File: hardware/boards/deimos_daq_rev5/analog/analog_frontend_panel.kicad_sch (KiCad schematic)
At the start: 17 parts, among them IC3001 BD42540FJ-CE2, IC3002 BD42540FJ-CE2, IC3003 BD42540FJ-CE2, J3001 Screw_Terminal_01x12, J3002 Screw_Terminal_01x10, J3003 Screw_Terminal_01x12, J3004 Screw_Terminal_01x12, J3005 Screw_Terminal_01x10, J3006 Screw_Terminal_01x12

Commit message: put +/12V on all inamps. add 3.3V zener behind first resistor of each filter.
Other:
- note added: "G=659+2/3"
- note removed: "G=666+1/3"
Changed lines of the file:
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@@
 		)
 	)
-	(text "G=666+1/3"
+	(text "G=659+2/3"
 		(exclude_from_sim no)
 		(at 265.684 70.866 0)

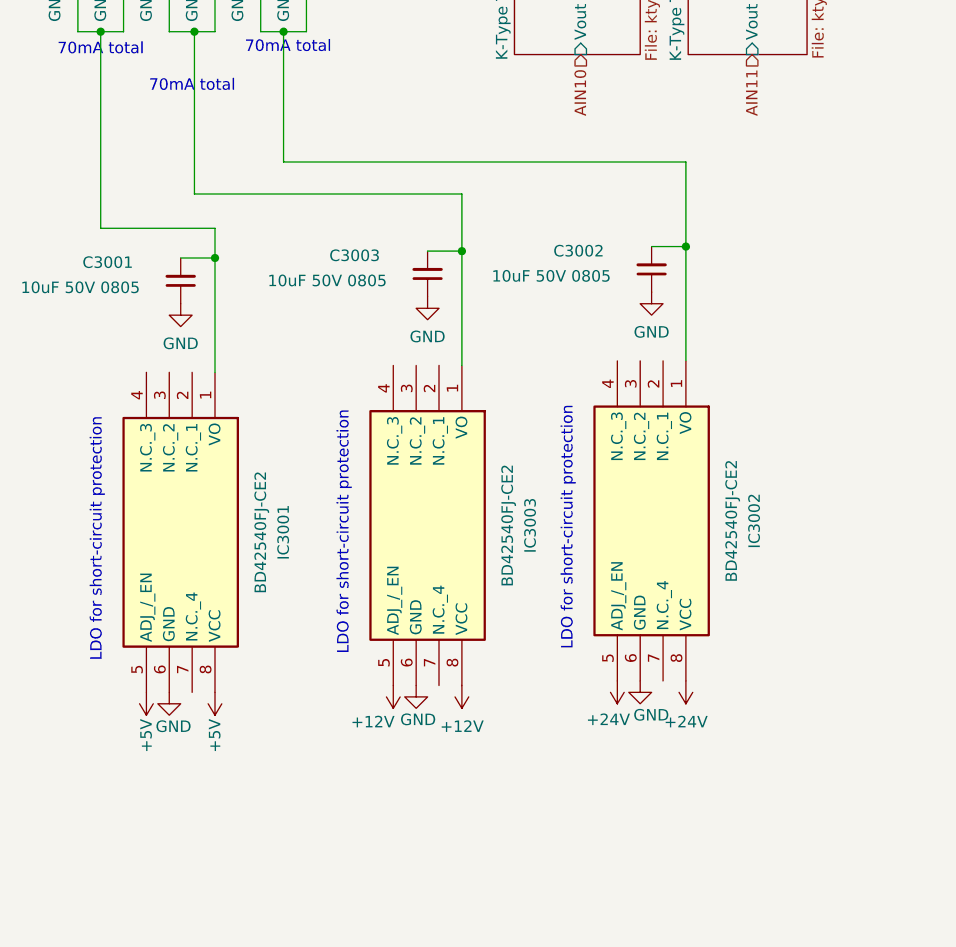
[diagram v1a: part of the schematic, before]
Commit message: add stabilizing integrator to current sinks
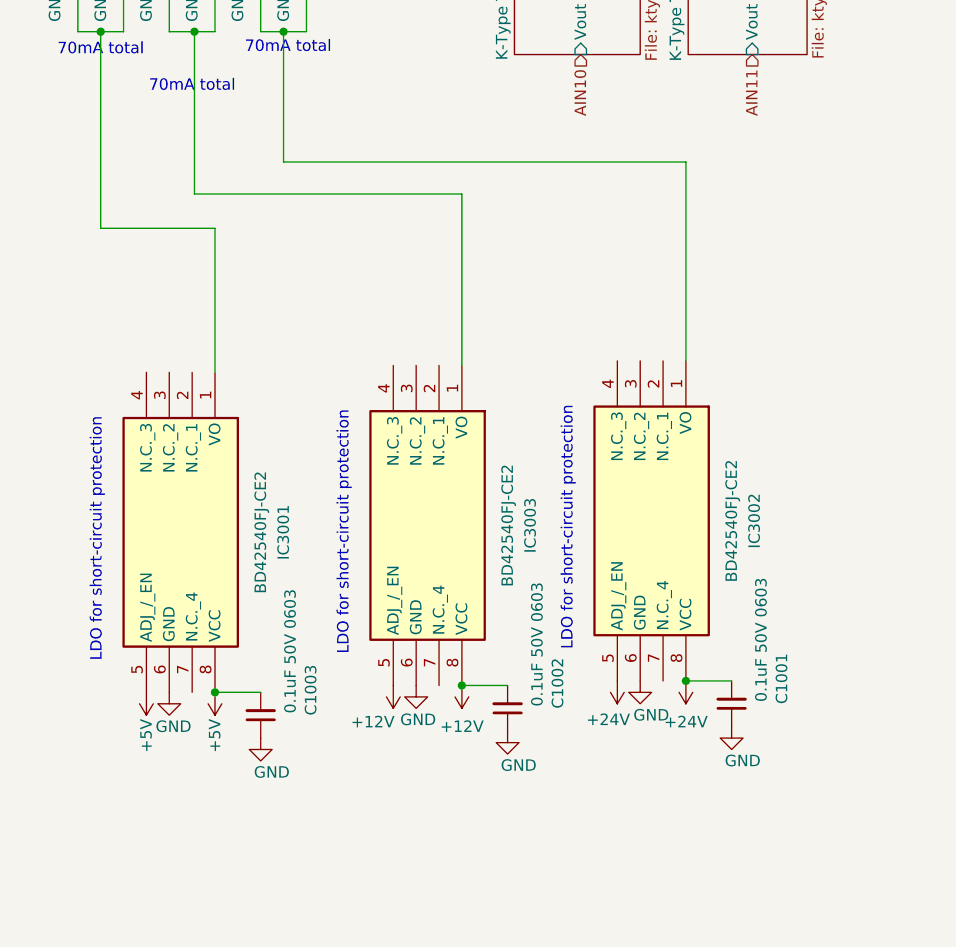
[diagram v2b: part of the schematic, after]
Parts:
- removed C3001, C3002, C3003: 10uF 50V 0805, Capacitor_SMD:C_0805_2012Metric, symbol Device:C_Small
- added C1001, C1002, C1003: 0.1uF 50V 0603, Capacitor_SMD:C_0603_1608Metric, symbol Device:C_Small
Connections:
- net +12V: now also C1002.2
- net +24V: now also C1001.2
- net +5V: now also C1003.2
- net GND: now also C1001.1, C1002.1, C1003.1

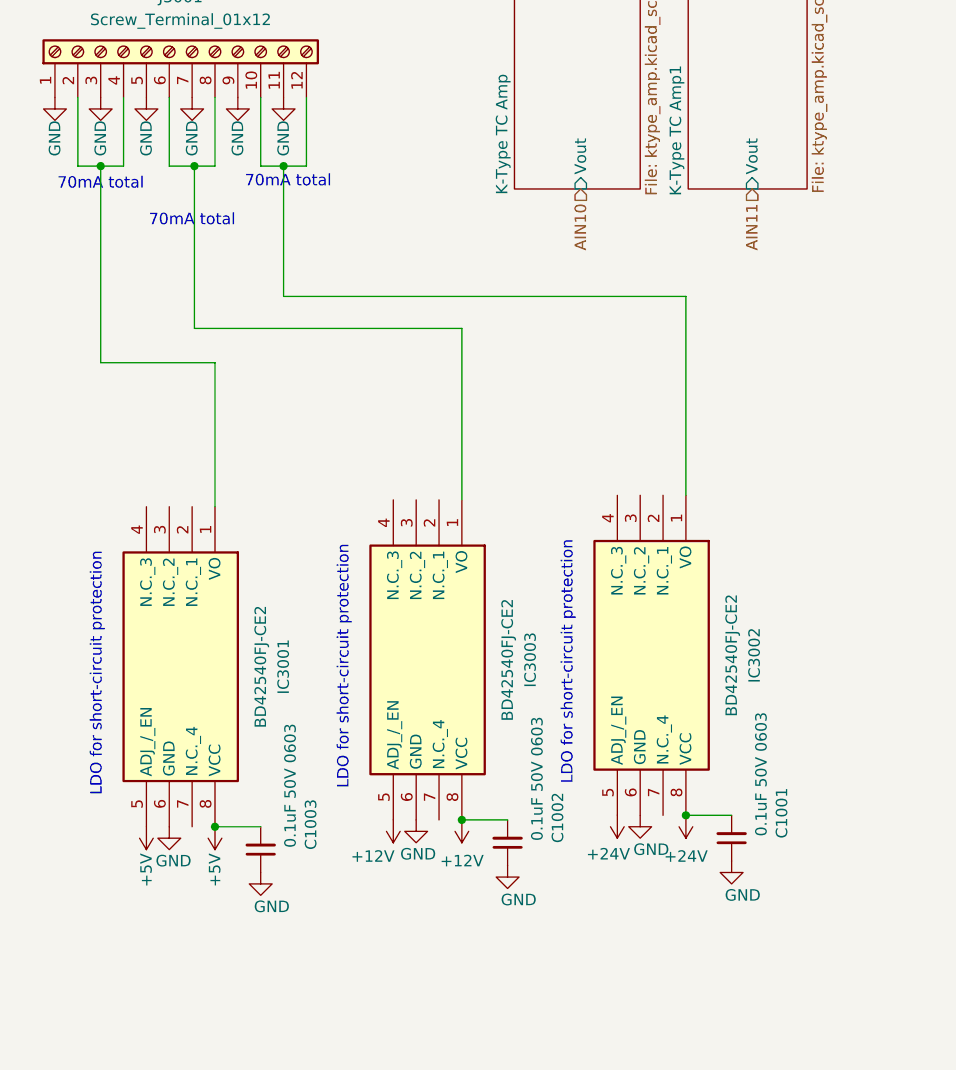
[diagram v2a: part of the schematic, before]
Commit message: eliminate 5V supply
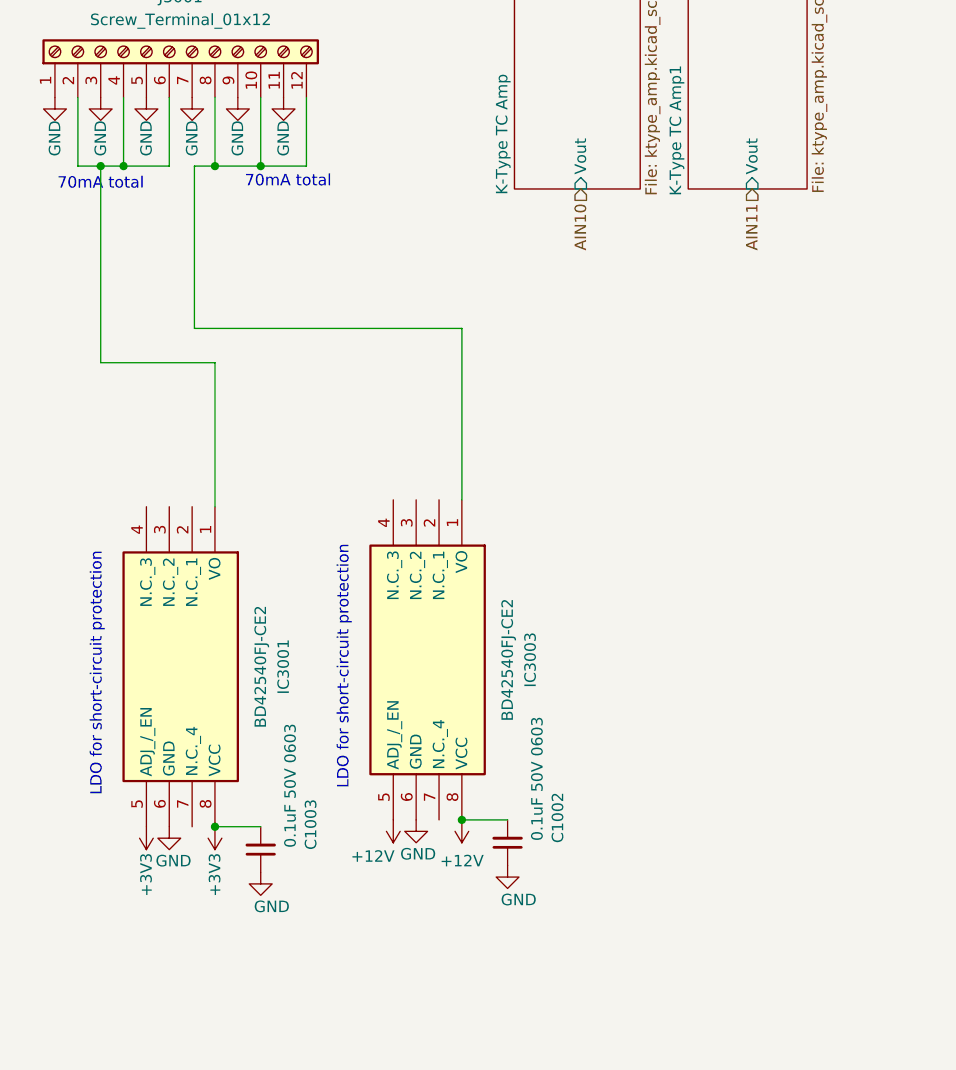
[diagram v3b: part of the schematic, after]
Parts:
- removed C1001: 0.1uF 50V 0603, Capacitor_SMD:C_0603_1608Metric, symbol Device:C_Small
- removed IC3002: BD42540FJ-CE2, aaa:SOIC127P600X175-8N, symbol aaa:BD42540FJ-CE2
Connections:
- net at J3001.10 (Pin_10), J3001.12 (Pin_12): now also IC3003.1 (VO), J3001.8 (Pin_8)
- net at IC3001.1 (VO), J3001.2 (Pin_2), J3001.4 (Pin_4): now also J3001.6 (Pin_6)
- net +5V renamed +3V3

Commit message: wip to update layout for voltage inputs
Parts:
- removed H3003, H3004: MountingHole_for_10-32, MountingHole:MountingHole_5mm, symbol Mechanical:MountingHole
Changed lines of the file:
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@@
-	)
-	(symbol
-		(lib_id "Mechanical:MountingHole")
-		(at 367.03 240.03 0)
-		(unit 1)
-		(exclude_from_sim no)
-		(in_bom no)
-		(on_board yes)
-		(dnp no)
-		(fields_autoplaced yes)
-		(property "Reference" "H3004"
-			(at 369.824 239.395 0)
-			(effects
-				(font
-					(size 1.27 1.27)
-				)
-				(justify left)
-			)
-		)
-		(property "Value" "MountingHole_for_10-32"
-			(at 369.824 241.935 0)
-			(effects
-				(font
-					(size 1.27 1.27)
-				)
-				(justify left)
-			)
-		)
-		(property "Footprint" "MountingHole:MountingHole_5mm"
-			(at 367.03 240.03 0)
-			(effects
-				(font
-					(size 1.27 1.27)
-				)
-				(hide yes)
-			)
-		)
-		(property "Datasheet" "~"
-			(at 367.03 240.03 0)
-			(effects
-				(font
-					(size 1.27 1.27)
-				)
-				(hide yes)
-			)
-		)
-		(property "Description" ""
-			(at 367.03 240.03 0)
-			(effects
-				(font
-					(size 1.27 1.27)
-				)
-				(hide yes)
-			)
-		)
-		(instances
-			(project "simplicity_analog_1"
-				(path "/5a60c4b1-b6cb-416e-8883-8291fa089b87/c2baf18d-2b19-4edb-98b3-535275ee271f"
-					(reference "H3004")
-					(unit 1)
-				)
-			)
-			(project "analog_frontend_panel"
-				(path "/c241d083-1323-4b4a-a540-956d0afb7b72"
-					(reference "H1004")
-					(unit 1)
-				)
-			)
-		)
 	)
 	(symbol
@@
 					(unit 1)
 				)
-			)
-		)
-	)
-	(symbol
-		(lib_id "Mechanical:MountingHole")
-		(at 367.03 234.442 0)
-		(unit 1)
-		(exclude_from_sim no)
-		(in_bom no)
-		(on_board yes)
-		(dnp no)
-		(fields_autoplaced yes)
-		(property "Reference" "H3003"
-			(at 369.824 233.807 0)
-			(effects
-				(font
-					(size 1.27 1.27)
-				)
-				(justify left)
-			)
-		)
-		(property "Value" "MountingHole_for_10-32"
-			(at 369.824 236.347 0)
-			(effects
-				(font
-					(size 1.27 1.27)
-				)
-				(justify left)
-			)
-		)
-		(property "Footprint" "MountingHole:MountingHole_5mm"
-			(at 367.03 234.442 0)
-			(effects
-				(font
-					(size 1.27 1.27)
-				)
-				(hide yes)
-			)
-		)
-		(property "Datasheet" "~"
-			(at 367.03 234.442 0)
-			(effects
-				(font
-					(size 1.27 1.27)
-				)
-				(hide yes)
-			)
-		)
-		(property "Description" ""
-			(at 367.03 234.442 0)
-			(effects
-				(font
-					(size 1.27 1.27)
-				)
-				(hide yes)
-			)
-		)
-		(instances
-			(project "simplicity_analog_1"
-				(path "/5a60c4b1-b6cb-416e-8883-8291fa089b87/c2baf18d-2b19-4edb-98b3-535275ee271f"
-					(reference "H3003")
-					(unit 1)
-				)
-			)
-			(project "analog_frontend_panel"
-				(path "/c241d083-1323-4b4a-a540-956d0afb7b72"
-					(reference "H1003")
-					(unit 1)
-				)

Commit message: restore rev5 and make this rev rev6
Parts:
- removed C1002, C1003: 0.1uF 50V 0603, Capacitor_SMD:C_0603_1608Metric, symbol Device:C_Small
- added C3001, C3002, C3003: 10uF 50V 0805, Capacitor_SMD:C_0805_2012Metric, symbol Device:C_Small
- added H3003, H3004: MountingHole_for_10-32, MountingHole:MountingHole_5mm, symbol Mechanical:MountingHole
- added IC3002: BD42540FJ-CE2, aaa:SOIC127P600X175-8N, symbol aaa:BD42540FJ-CE2
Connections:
- net +12V: no longer IC3003.5 (ADJ_/_EN)
- net GND: now also IC3001.5 (ADJ_/_EN), IC3003.5 (ADJ_/_EN), C3001.1, C3002.1, C3003.1, IC3002.5 (ADJ_/_EN), IC3002.6 (GND)
- net at J3001.10 (Pin_10), J3001.12 (Pin_12): now also C3002.2, IC3002.1 (VO); no longer IC3003.1 (VO), J3001.8 (Pin_8)
- net at IC3001.1 (VO), J3001.2 (Pin_2), J3001.4 (Pin_4): now also C3001.2; no longer J3001.6 (Pin_6)
- net +3V3 renamed +5V
- net +5V: no longer IC3001.5 (ADJ_/_EN)
- new net: C3003.2, IC3003.1 (VO), J3001.6 (Pin_6), J3001.8 (Pin_8)
- new net +24V: IC3002.8 (VCC)
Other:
- note added: "G=666+1/3"
- note added: "Short fb to gnd for pass-through"
- note removed: "G=659+2/3"

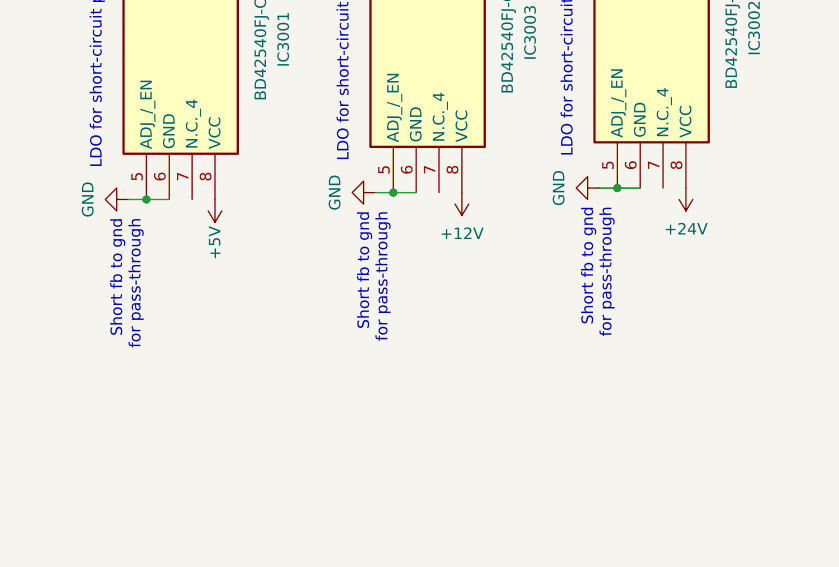
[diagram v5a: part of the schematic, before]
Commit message: fix ldos
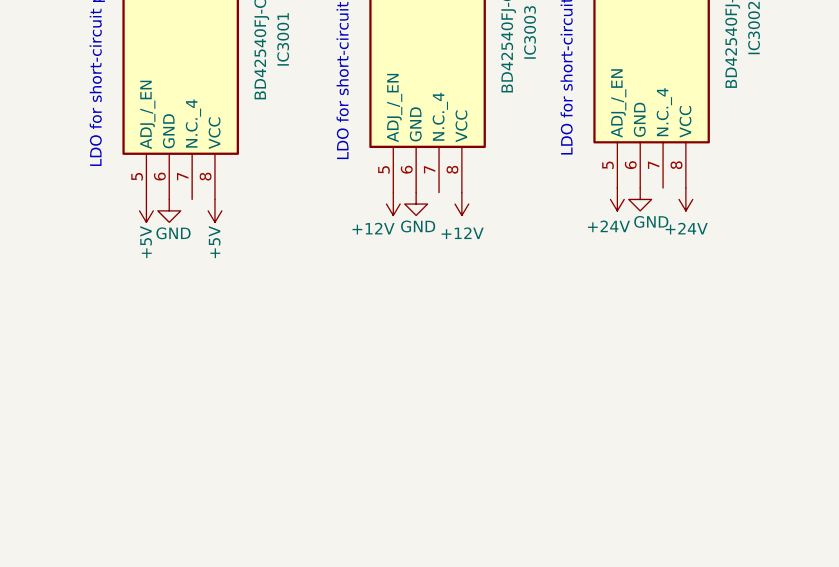
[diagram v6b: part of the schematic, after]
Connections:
- net +12V: now also IC3003.5 (ADJ_/_EN)
- net +24V: now also IC3002.5 (ADJ_/_EN)
- net +5V: now also IC3001.5 (ADJ_/_EN)
- net GND: no longer IC3001.5 (ADJ_/_EN), IC3002.5 (ADJ_/_EN), IC3003.5 (ADJ_/_EN)
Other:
- note removed: "Short fb to gnd for pass-through"
